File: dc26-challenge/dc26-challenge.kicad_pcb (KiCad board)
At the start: 2 copper layers, 107 x 107 mm, 0 parts

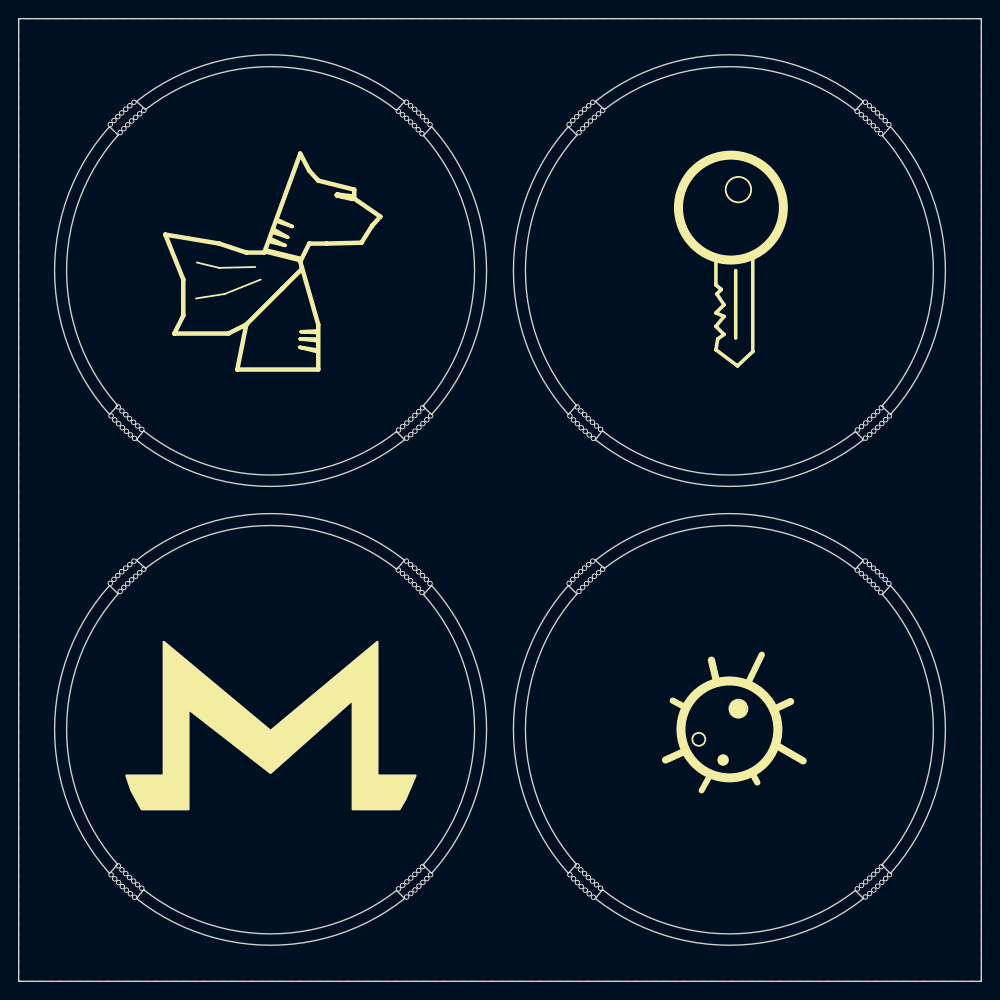
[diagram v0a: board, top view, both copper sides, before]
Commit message: NPTH drill holes for snaps
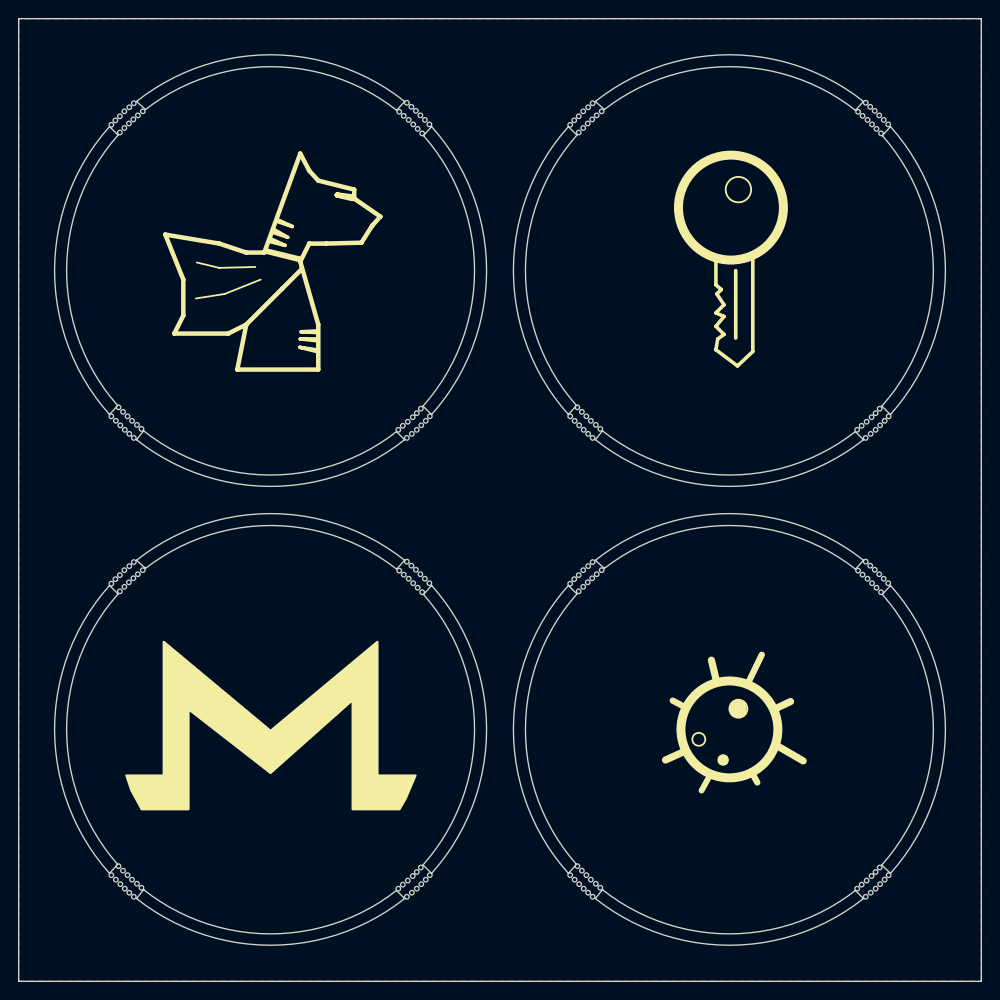
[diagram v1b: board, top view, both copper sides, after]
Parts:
- added ?: , snap:snap, F.Cu at (107.2, 54.6)
- added ?: , snap:snap, F.Cu at (107.8, 54.1)
- added ?: , snap:snap, F.Cu at (91.3, 103.2)
- added ?: , snap:snap, F.Cu at (57.8, 104.2)
- added ?: , snap:snap, F.Cu at (57.3, 139.2)
- added ?: , snap:snap, F.Cu at (57.8, 139.7)
- added ?: , snap:snap, F.Cu at (59.1, 139.2)
- added ?: , snap:snap, F.Cu at (55.8, 104.3)
- added ?: , snap:snap, F.Cu at (56.8, 105.2)
- added ?: , snap:snap, F.Cu at (91.2, 138.7)
- added ?: , snap:snap, F.Cu at (56.8, 103.3)
- added ?: , snap:snap, F.Cu at (91.7, 101.8)
- added ?: , snap:snap, F.Cu at (142.2, 87.7)
- added ?: , snap:snap, F.Cu at (92.7, 102.8)
- added ?: , snap:snap, F.Cu at (57.8, 102.4)
- added ?: , snap:snap, F.Cu at (56.2, 103.8)
- added ?: , snap:snap, F.Cu at (91.8, 103.8)
- added ?: , snap:snap, F.Cu at (89.8, 101.8)
- added ?: , snap:snap, F.Cu at (92.8, 137.3)
- added ?: , snap:snap, F.Cu at (58.8, 140.7)
- added ?: , snap:snap, F.Cu at (94.2, 137.7)
- added ?: , snap:snap, F.Cu at (58.8, 103.3)
- added ?: , snap:snap, F.Cu at (90.3, 102.2)
- added ?: , snap:snap, F.Cu at (107.8, 52.3)
- added ?: , snap:snap, F.Cu at (92.2, 137.8)
- added ?: , snap:snap, F.Cu at (91.2, 101.2)
- added ?: , snap:snap, F.Cu at (90.7, 100.8)
- added ?: , snap:snap, F.Cu at (92.7, 139.2)
- added ?: , snap:snap, F.Cu at (94.7, 137.2)
- added ?: , snap:snap, F.Cu at (58.3, 140.2)
- added ?: , snap:snap, F.Cu at (59.6, 139.7)
- added ?: , snap:snap, F.Cu at (59.8, 141.6)
- added ?: , snap:snap, F.Cu at (60.6, 140.6)
- added ?: , snap:snap, F.Cu at (93.2, 138.7)
- added ?: , snap:snap, F.Cu at (142.7, 50.8)
- added ?: , snap:snap, F.Cu at (59.3, 141.2)
- added ?: , snap:snap, F.Cu at (58.6, 138.7)
- added ?: , snap:snap, F.Cu at (58.2, 103.8)
- added ?: , snap:snap, F.Cu at (57.2, 104.7)
- added ?: , snap:snap, F.Cu at (57.3, 102.8)
- added ?: , snap:snap, F.Cu at (93.2, 136.8)
- added ?: , snap:snap, F.Cu at (55.3, 104.8)
- added ?: , snap:snap, F.Cu at (92.2, 102.2)
- added ?: , snap:snap, F.Cu at (89.3, 101.3)
- added ?: , snap:snap, F.Cu at (60.1, 140.2)
- added ?: , snap:snap, F.Cu at (143.7, 51.8)
- added ?: , snap:snap, F.Cu at (93.7, 136.3)
- added ?: , snap:snap, F.Cu at (58.1, 138.2)
- added ?: , snap:snap, F.Cu at (91.7, 138.2)
- added ?: , snap:snap, F.Cu at (93.8, 138.2)
- added ?: , snap:snap, F.Cu at (92.2, 139.6)
- added ?: , snap:snap, F.Cu at (145.7, 137.2)
- added ?: , snap:snap, F.Cu at (143.2, 137.8)
- added ?: , snap:snap, F.Cu at (142.7, 138.2)
- added ?: , snap:snap, F.Cu at (144.2, 138.7)
- added ?: , snap:snap, F.Cu at (143.2, 139.6)
- added ?: , snap:snap, F.Cu at (108.8, 51.4)
- added ?: , snap:snap, F.Cu at (142.2, 138.7)
- added ?: , snap:snap, F.Cu at (144.2, 136.8)
- added ?: , snap:snap, F.Cu at (143.8, 137.3)
- added ?: , snap:snap, F.Cu at (144.8, 138.2)
- added ?: , snap:snap, F.Cu at (145.2, 137.7)
- added ?: , snap:snap, F.Cu at (143.7, 139.2)
- added ?: , snap:snap, F.Cu at (144.7, 136.3)
- added ?: , snap:snap, F.Cu at (110.8, 141.6)
- added ?: , snap:snap, F.Cu at (110.1, 139.2)
- added ?: , snap:snap, F.Cu at (109.6, 138.7)
- added ?: , snap:snap, F.Cu at (107.2, 52.9)
- added ?: , snap:snap, F.Cu at (109.3, 140.2)
- added ?: , snap:snap, F.Cu at (108.3, 139.2)
- added ?: , snap:snap, F.Cu at (109.1, 138.2)
- added ?: , snap:snap, F.Cu at (111.2, 140.2)
- added ?: , snap:snap, F.Cu at (110.6, 139.7)
- added ?: , snap:snap, F.Cu at (109.8, 140.7)
- added ?: , snap:snap, F.Cu at (110.3, 141.2)
- added ?: , snap:snap, F.Cu at (108.8, 139.7)
- added ?: , snap:snap, F.Cu at (111.7, 140.6)
- added ?: , snap:snap, F.Cu at (106.3, 104.8)
- added ?: , snap:snap, F.Cu at (142.8, 52.8)
- added ?: , snap:snap, F.Cu at (108.8, 104.2)
- added ?: , snap:snap, F.Cu at (109.2, 103.8)
- added ?: , snap:snap, F.Cu at (107.8, 103.3)
- added ?: , snap:snap, F.Cu at (108.8, 102.4)
- added ?: , snap:snap, F.Cu at (109.8, 103.3)
- added ?: , snap:snap, F.Cu at (107.8, 105.2)
- added ?: , snap:snap, F.Cu at (108.2, 104.7)
- added ?: , snap:snap, F.Cu at (107.2, 103.8)
- added ?: , snap:snap, F.Cu at (106.8, 104.3)
- added ?: , snap:snap, F.Cu at (108.3, 102.8)
- added ?: , snap:snap, F.Cu at (140.8, 50.8)
- added ?: , snap:snap, F.Cu at (107.2, 105.7)
- added ?: , snap:snap, F.Cu at (142.8, 103.8)
- added ?: , snap:snap, F.Cu at (142.3, 103.2)
- added ?: , snap:snap, F.Cu at (141.8, 102.8)
- added ?: , snap:snap, F.Cu at (141.3, 102.2)
- added ?: , snap:snap, F.Cu at (140.8, 101.8)
- added ?: , snap:snap, F.Cu at (140.3, 101.3)
- added ?: , snap:snap, F.Cu at (143.7, 102.8)
- added ?: , snap:snap, F.Cu at (143.2, 102.2)
- added ?: , snap:snap, F.Cu at (142.7, 101.8)
- added ?: , snap:snap, F.Cu at (143.8, 86.3)
- added ?: , snap:snap, F.Cu at (142.2, 101.2)
- added ?: , snap:snap, F.Cu at (141.7, 100.8)
- added ?: , snap:snap, F.Cu at (141.2, 100.3)
- added ?: , snap:snap, F.Cu at (141.2, 49.4)
- added ?: , snap:snap, F.Cu at (109.8, 89.7)
- added ?: , snap:snap, F.Cu at (145.2, 86.7)
- added ?: , snap:snap, F.Cu at (109.8, 52.3)
- added ?: , snap:snap, F.Cu at (141.3, 51.2)
- added ?: , snap:snap, F.Cu at (143.2, 86.8)
- added ?: , snap:snap, F.Cu at (142.2, 50.2)
- added ?: , snap:snap, F.Cu at (141.7, 49.8)
- added ?: , snap:snap, F.Cu at (143.7, 88.2)
- added ?: , snap:snap, F.Cu at (145.7, 86.2)
- added ?: , snap:snap, F.Cu at (109.3, 89.2)
- added ?: , snap:snap, F.Cu at (141.8, 51.8)
- added ?: , snap:snap, F.Cu at (110.6, 88.7)
- added ?: , snap:snap, F.Cu at (110.8, 90.6)
- added ?: , snap:snap, F.Cu at (111.7, 89.6)
- added ?: , snap:snap, F.Cu at (144.2, 87.7)
- added ?: , snap:snap, F.Cu at (110.3, 90.2)
- added ?: , snap:snap, F.Cu at (109.6, 87.7)
- added ?: , snap:snap, F.Cu at (109.2, 52.8)
- added ?: , snap:snap, F.Cu at (108.2, 53.6)
- added ?: , snap:snap, F.Cu at (108.3, 51.9)
- added ?: , snap:snap, F.Cu at (144.2, 85.8)
- added ?: , snap:snap, F.Cu at (142.3, 52.2)
- added ?: , snap:snap, F.Cu at (106.3, 53.8)
- added ?: , snap:snap, F.Cu at (143.2, 51.2)
- added ?: , snap:snap, F.Cu at (140.3, 50.4)
- added ?: , snap:snap, F.Cu at (111.2, 89.2)
- added ?: , snap:snap, F.Cu at (144.7, 85.3)
- added ?: , snap:snap, F.Cu at (109.1, 87.2)
- added ?: , snap:snap, F.Cu at (142.7, 87.2)
- added ?: , snap:snap, F.Cu at (144.8, 87.2)
- added ?: , snap:snap, F.Cu at (143.2, 88.6)
- added ?: , snap:snap, F.Cu at (56.2, 54.6)
- added ?: , snap:snap, F.Cu at (108.8, 53.2)
- added ?: , snap:snap, F.Cu at (90.2, 49.4)
- added ?: , snap:snap, F.Cu at (90.8, 51.8)
- added ?: , snap:snap, F.Cu at (91.3, 52.2)
- added ?: , snap:snap, F.Cu at (57.8, 53.2)
- added ?: , snap:snap, F.Cu at (57.3, 88.2)
- added ?: , snap:snap, F.Cu at (57.8, 88.7)
- added ?: , snap:snap, F.Cu at (59.1, 88.2)
- added ?: , snap:snap, F.Cu at (55.8, 53.3)
- added ?: , snap:snap, F.Cu at (56.8, 54.1)
- added ?: , snap:snap, F.Cu at (91.2, 87.7)
- added ?: , snap:snap, F.Cu at (108.3, 88.2)
- added ?: , snap:snap, F.Cu at (56.8, 52.3)
- added ?: , snap:snap, F.Cu at (91.7, 50.8)
- added ?: , snap:snap, F.Cu at (92.7, 51.8)
- added ?: , snap:snap, F.Cu at (57.8, 51.4)
- added ?: , snap:snap, F.Cu at (56.2, 52.9)
- added ?: , snap:snap, F.Cu at (91.8, 52.8)
- added ?: , snap:snap, F.Cu at (89.8, 50.8)
- added ?: , snap:snap, F.Cu at (92.8, 86.3)
- added ?: , snap:snap, F.Cu at (58.8, 89.7)
- added ?: , snap:snap, F.Cu at (94.2, 86.7)
- added ?: , snap:snap, F.Cu at (108.8, 88.7)
- added ?: , snap:snap, F.Cu at (58.8, 52.3)
- added ?: , snap:snap, F.Cu at (90.3, 51.2)
- added ?: , snap:snap, F.Cu at (92.2, 86.8)
- added ?: , snap:snap, F.Cu at (91.2, 50.2)
- added ?: , snap:snap, F.Cu at (90.7, 49.8)
- added ?: , snap:snap, F.Cu at (92.7, 88.2)
- added ?: , snap:snap, F.Cu at (94.7, 86.2)
- added ?: , snap:snap, F.Cu at (58.3, 89.2)
- added ?: , snap:snap, F.Cu at (59.6, 88.7)
- added ?: , snap:snap, F.Cu at (59.8, 90.6)
- added ?: , snap:snap, F.Cu at (110.1, 88.2)
- added ?: , snap:snap, F.Cu at (60.6, 89.6)
- added ?: , snap:snap, F.Cu at (93.2, 87.7)
- added ?: , snap:snap, F.Cu at (59.3, 90.2)
- added ?: , snap:snap, F.Cu at (58.6, 87.7)
- added ?: , snap:snap, F.Cu at (58.2, 52.8)
- added ?: , snap:snap, F.Cu at (57.2, 53.6)
- added ?: , snap:snap, F.Cu at (57.3, 51.9)
- added ?: , snap:snap, F.Cu at (93.2, 85.8)
- added ?: , snap:snap, F.Cu at (55.3, 53.8)
- added ?: , snap:snap, F.Cu at (92.2, 51.2)
- added ?: , snap:snap, F.Cu at (106.8, 53.3)
- added ?: , snap:snap, F.Cu at (89.3, 50.4)
- added ?: , snap:snap, F.Cu at (60.1, 89.2)
- added ?: , snap:snap, F.Cu at (93.7, 85.3)
- added ?: , snap:snap, F.Cu at (58.1, 87.2)
- added ?: , snap:snap, F.Cu at (91.7, 87.2)
- added ?: , snap:snap, F.Cu at (93.8, 87.2)
- added ?: , snap:snap, F.Cu at (92.2, 88.6)
- added ?: , snap:snap, F.Cu at (56.2, 105.7)
- added ?: , snap:snap, F.Cu at (90.2, 100.3)
- added ?: , snap:snap, F.Cu at (90.8, 102.8)
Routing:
- net (no net): vias 224 -> 0
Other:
- board text added: "33, 17, 15, 13, 13, 0d, 47, 08, 13, 1e, 09, 1f, 0c, 50, 11, 04, 06, 47, 12, 52, 1b, 11, 1a, 08, 05, 45, 50, 04, 02, 07, 47, 11, 54, 0f, 16, 17, 41, 09, 46, 50, 0d, 05, 07, 0e, 0c, 47, 5a, 1b, 00, 07, 09, 52, 1d, 04, 18, 0a, 08, 0c"
- board text removed: "33, 17, 15, 13, 13, 0d, 47, 08, 13, 1e, 09, 1f, 0c, 50, 11, 04, 06, 47, 12, 52, 1b, 11, 1a, 08, 05, 45, 50, 04, 02, 07, 47, 11, 54, 0f, 16, 17, 41, 09, 46, 50, 0d, 05, 07, 0e, 0c, 47, 5a, 1b, 00, 07, 09, 52, 1d, 04, 18, 0a, 8, 0c"

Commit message: Fixed bad crypto
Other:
- board text added: "20, 00, 00, 00, 00, 00, 43, 18, 17, 13, 0b, 1d, 43, 1a, 5e, 59, 14, 1d, 08, 49, 19, 04, 0d, 4e, 10, 55, 11, 00, 1c, 1e, 17, 16, 00, 19, 0d, 00, 1a, 53, 16, 01, 1c, 03, 54, 0c, 52, 14, 15, 15, 01, 14, 52, 02, 02, 11, 09, 54, 1b, 4f, 4d, 16, 04, 0d, 06, 52, 06, 52, 0d, 02, 15, 01, 53, 0c, 06, 15, 07, 1c, 0d, 01"
- board text added: "20, 00, 00, 00, 00, 00, 47, 1f, 04, 11, 06, 0a, 0c, 43, 06, 11, 15, 54, 1f, 52, 0c, 06, 15, 07, 10, 45, 43, 13, 17, 14, 54, 1c, 54, 18, 01, 18, 4e, 1c, 05, 52, 11, 19, 10, 06, 4e, 0a, 45, 08, 00, 15, 4f, 11, 1f, 18, 04, 1d, 00, 4e"
- board text added: "20, 00, 00, 00, 00, 00, 53, 1d, 0a, 13, 07, 17, 49, 16, 1f, 55, 50, 15, 4f, 50, 1f, 0a, 15, 01, 09, 4f, 02, 1c, 59, 04, 1c, 0e, 54, 4d, 06, 00, 00, 53, 00, 13, 0c, 3, 11, 4f, 47, 0c, 16, 15, 1c, 1c, 0d, 0a, 1c, 0d, 15, 07, 1b, 49, 03, 04, 0d, 4e, 1a, 4c, 0f, 1c, 1c, 03, 07, 4f, 57, 04, 11, 09, 4e, 17, 0a, 13, 0b, 02, 1c, 0a, 41, 4d, 0c, 0f, 4e, 1b, 55, 0e, 13, 17, 03"
- board text added: "28, 00, 00, 00, 00, 00, 0c, 4d, 36, 14, 1e, 16, 52, 0e, 13, 17, 57, 07, 4f, 50, 08, 11, 41, 0a, 1c, 47, 43, 1b, 17, 50, 00, 07, 45, 4d, 15, 0e, 1e, 06, 0f, 13, 0b, 50, 17, 00, 4d, 04, 06, 4d, 4e, 10, 41, 11, 06, 16, 1f, 1a, 43, 00, 0c, 0b, 05, 4e, 1e, 4f, 15, 1b, 1c, 50, 07, 0a, 52, 04, 00, 12"
- board text removed: "33, 17, 15, 13, 13, 0d, 43, 0f, 00, 1c, 04, 08, 43, 09, 49, 4c, 07, 0e, 05, 49, 0e, 13, 02, 41, 05, 55, 02, 17, 09, 0d, 04, 1b, 00, 0e, 1a, 0f, 15, 46, 55, 03, 00, 1f, 43, 04, 10, 59, 0a, 06, 01, 06, 14, 41, 00, 0d, 15, 43, 13, 0d, 00, 09, 17, 0d, 14, 14, 45, 50, 11, 1e, 02, 09, 11, 41, 19, 06, 07, 0e, 08, 53"
- board text removed: "33, 17, 15, 13, 13, 0d, 47, 08, 13, 1e, 09, 1f, 0c, 50, 11, 04, 06, 47, 12, 52, 1b, 11, 1a, 08, 05, 45, 50, 04, 02, 07, 47, 11, 54, 0f, 16, 17, 41, 09, 46, 50, 0d, 05, 07, 0e, 0c, 47, 5a, 1b, 00, 07, 09, 52, 1d, 04, 18, 0a, 08, 0c"
- board text removed: "33, 17, 15, 13, 13, 0d, 53, 0a, 1d, 1c, 08, 02, 49, 05, 08, 40, 43, 06, 42, 50, 08, 1d, 1a, 0e, 1c, 4f, 11, 0b, 4c, 17, 0f, 03, 54, 5a, 11, 0f, 0f, 46, 43, 11, 10, 1f, 06, 47, 05, 41, 09, 06, 1c, 0e, 4b, 49, 1e, 11, 09, 10, 13, 0b, 4e, 1b, 1e, 4e, 08, 0a, 4c, 1e, 00, 1f, 10, 47, 15, 49, 0e, 1a, 4e, 05, 0f, 41, 02, 17, 04, 06, 06, 42, 49, 14, 52, 06, 14, 0b, 41, 1e, 16"
- board text removed: "3b, 17, 15, 13, 13, 0d, 0c, 5a, 21, 1b, 11, 03, 52, 1d, 04, 02, 44, 14, 42, 50, 1f, 06, 4e, 05, 09, 47, 50, 0c, 02, 43, 13, 0a, 45, 5a, 02, 01, 11, 13, 4c, 11, 17, 4c, 00, 08, 0f, 49, 19, 5e, 4e, 02, 07, 52, 04, 0a, 03, 0d, 4b, 42, 41, 14, 16, 4e, 0c, 09, 56, 19, 00, 4c, 10, 02, 10, 49, 1f, 01"
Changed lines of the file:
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@@
   (page A4)
   (layers
-    (0 F.Cu signal)
+    (0 F.Cu signal hide)
     (31 B.Cu signal)
     (32 B.Adhes user)
@@
     (pad "" np_thru_hole circle (at 0 2) (size 0.5 0.5) (drill 0.5) (layers *.Cu *.Mask))
   )
-  (gr_text "33, 17, 15, 13, 13, 0d, 53, 0a, \n1d, 1c, 08, 02, 49, 05, 08, 40, \n43, 06, 42, 50, 08, 1d, 1a, 0e, \n1c, 4f, 11, 0b, 4c, 17, 0f, 03, \n54, 5a, 11, 0f, 0f, 46, 43, 11, \n10, 1f, 06, 47, 05, 41, 09, 06, \n1c, 0e, 4b, 49, 1e, 11, 09, 10, \n13, 0b, 4e, 1b, 1e, 4e, 08, 0a, \n4c, 1e, 00, 1f, 10, 47, 15, 49, \n0e, 1a, 4e, 05, 0f, 41, 02, 17, \n04, 06, 06, 42, 49, 14, 52, 06, \n14, 0b, 41, 1e, 16" (at 125 120.6) (layer B.SilkS)
+  (gr_text "20, 00, 00, 00, 00, 00, 53, 1d, \n0a, 13, 07, 17, 49, 16, 1f, 55, \n50, 15, 4f, 50, 1f, 0a, 15, 01,\n 09, 4f, 02, 1c, 59, 04, 1c, 0e, \n54, 4d, 06, 00, 00, 53, 00, 13, \n0c, 3, 11, 4f, 47, 0c, 16, 15, \n1c, 1c, 0d, 0a, 1c, 0d, 15, 07, \n1b, 49, 03, 04, 0d, 4e, 1a, 4c, \n0f, 1c, 1c, 03, 07, 4f, 57, 04, \n11, 09, 4e, 17, 0a, 13, 0b, 02, \n1c, 0a, 41, 4d, 0c, 0f, 4e, 1b, \n55, 0e, 13, 17, 03" (at 125 120.6) (layer B.SilkS)
     (effects (font (size 1.3 1.5) (thickness 0.25)) (justify mirror))
   )
-  (gr_text "33, 17, 15, 13, 13, 0d, 43, 0f, \n00, 1c, 04, 08, 43, 09, 49, 4c, \n07, 0e, 05, 49, 0e, 13, 02, 41, \n05, 55, 02, 17, 09, 0d, 04, 1b, \n00, 0e, 1a, 0f, 15, 46, 55, 03, \n00, 1f, 43, 04, 10, 59, 0a, 06, \n01, 06, 14, 41, 00, 0d, 15, 43, \n13, 0d, 00, 09, 17, 0d, 14, 14, \n45, 50, 11, 1e, 02, 09, 11, 41, \n19, 06, 07, 0e, 08, 53" (at 74.2 120.4) (layer B.SilkS)
+  (gr_text "20, 00, 00, 00, 00, 00, 43, 18, \n17, 13, 0b, 1d, 43, 1a, 5e, 59, \n14, 1d, 08, 49, 19, 04, 0d, 4e, \n10, 55, 11, 00, 1c, 1e, 17, 16, \n00, 19, 0d, 00, 1a, 53, 16, 01, \n1c, 03, 54, 0c, 52, 14, 15, 15, \n01, 14, 52, 02, 02, 11, 09, 54, \n1b, 4f, 4d, 16, 04, 0d, 06, 52, \n06, 52, 0d, 02, 15, 01, 53, 0c, \n06, 15, 07, 1c, 0d, 01" (at 74.2 120.4) (layer B.SilkS)
     (effects (font (size 1.5 1.5) (thickness 0.25)) (justify mirror))
   )
-  (gr_text "33, 17, 15, 13, 13, 0d, 47, 08, \n13, 1e, 09, 1f, 0c, 50, 11, 04, \n06, 47, 12, 52, 1b, 11, 1a, 08, \n05, 45, 50, 04, 02, 07, 47, 11, \n54, 0f, 16, 17, 41, 09, 46, 50, \n0d, 05, 07, 0e, 0c, 47, 5a, 1b, \n00, 07, 09, 52, 1d, 04, 18, 0a, \n08, 0c" (at 125.7 69.9) (layer B.SilkS)
+  (gr_text "20, 00, 00, 00, 00, 00, 47, 1f, \n04, 11, 06, 0a, 0c, 43, 06, 11, \n15, 54, 1f, 52, 0c, 06, 15, 07, \n10, 45, 43, 13, 17, 14, 54, 1c, \n54, 18, 01, 18, 4e, 1c, 05, 52, \n11, 19, 10, 06, 4e, 0a, 45, 08, \n00, 15, 4f, 11, 1f, 18, 04, 1d, \n00, 4e" (at 125.7 69.9) (layer B.SilkS)
     (effects (font (size 1.5 1.5) (thickness 0.25)) (justify mirror))
   )
@@
     (effects (font (size 1.5 1.5) (thickness 0.3)) (justify mirror))
   )
-  (gr_text "3b, 17, 15, 13, 13, 0d, 0c, 5a, \n21, 1b, 11, 03, 52, 1d, 04, 02, \n44, 14, 42, 50, 1f, 06, 4e, 05, \n09, 47, 50, 0c, 02, 43, 13, 0a, \n45, 5a, 02, 01, 11, 13, 4c, 11, \n17, 4c, 00, 08, 0f, 49, 19, 5e, \n4e, 02, 07, 52, 04, 0a, 03, 0d, \n4b, 42, 41, 14, 16, 4e, 0c, 09, \n56, 19, 00, 4c, 10, 02, 10, 49, \n1f, 01" (at 74.4 69.9) (layer B.SilkS)
+  (gr_text "28, 00, 00, 00, 00, 00, 0c, 4d, \n36, 14, 1e, 16, 52, 0e, 13, 17, \n57, 07, 4f, 50, 08, 11, 41, 0a, \n1c, 47, 43, 1b, 17, 50, 00, 07, \n45, 4d, 15, 0e, 1e, 06, 0f, 13, \n0b, 50, 17, 00, 4d, 04, 06, 4d, \n4e, 10, 41, 11, 06, 16, 1f, 1a, \n43, 00, 0c, 0b, 05, 4e, 1e, 4f, \n15, 1b, 1c, 50, 07, 0a, 52, 04, \n00, 12" (at 74.4 69.9) (layer B.SilkS)
     (effects (font (size 1.5 1.5) (thickness 0.25)) (justify mirror))
   )
